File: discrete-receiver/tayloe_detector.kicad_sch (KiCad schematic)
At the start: 22 parts, among them U1 SN74CBT3253DBQR, U2 OPA1612AxD, U3 OPA1612AxD

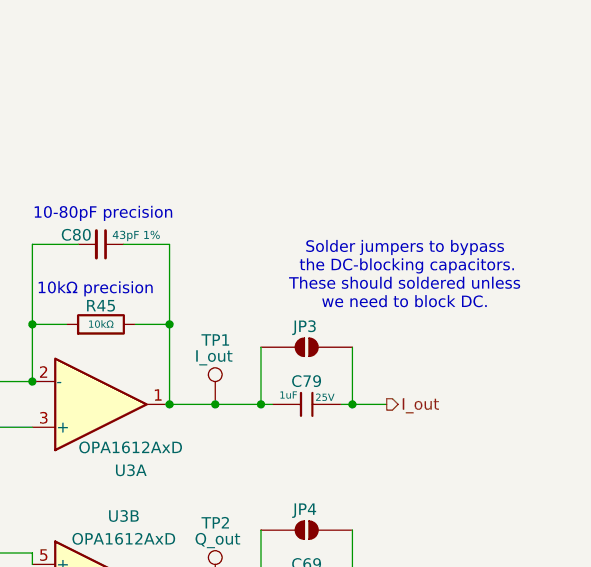
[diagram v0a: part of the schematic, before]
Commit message: Subsheetified the receiver page
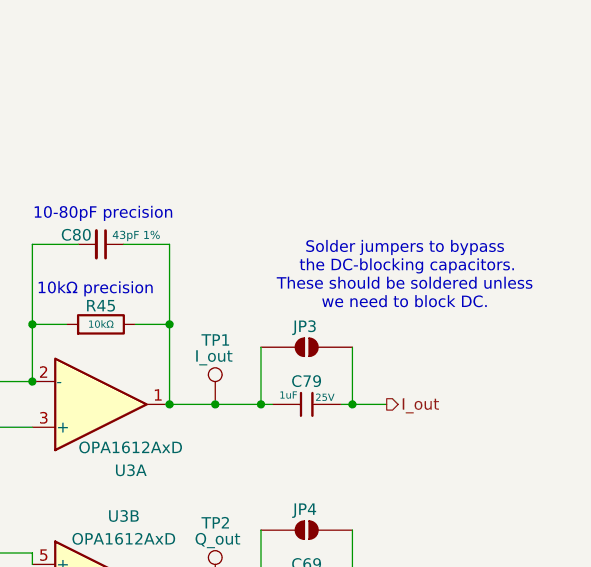
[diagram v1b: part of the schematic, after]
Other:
- note added: "Solder jumpers to bypass the DC-blocking capacitors. These should be soldered unless we need to block DC."
- note removed: "Solder jumpers to bypass the DC-blocking capacitors. These should soldered unless we need to block DC."
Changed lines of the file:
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@@
 		)
 	)
-	(text "Solder jumpers to bypass\n the DC-blocking capacitors.\nThese should soldered unless \nwe need to block DC."
+	(text "Solder jumpers to bypass\n the DC-blocking capacitors.\nThese should be soldered unless \nwe need to block DC."
 		(exclude_from_sim no)
 		(at 226.822 75.946 0)

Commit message: Progress made on schematic
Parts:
- added C8, C83: 100nF, PCM_JLCPCB:C_0402, symbol PCM_JLCPCB-Capacitors:0402,100nF
- added C82, C84: 1uF, PCM_JLCPCB:C_0402, symbol PCM_JLCPCB-Capacitors:0402,1uF
- added JP19, JP23, JP24, JP25: SolderJumper_2_Open, symbol Jumper:SolderJumper_2_Open
- added R48, R49: 10kΩ, PCM_JLCPCB:R_0402, symbol PCM_JLCPCB-Resistors:0402,10kΩ
- added unit 3 of U2
- added unit 3 of U3
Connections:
- net GND: now also C8.2, C82.2, C83.2, C84.2, U2.4 (V-), U3.4 (V-)
- net at C79.1, C80.1, JP3.2 (B)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: now also R48.2
- net at R14.2, R45.1, U3.2 (-): now also JP19.2 (B), JP23.2 (B); no longer C80.2
- net at C69.1, C81.1, JP4.2 (B)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: now also R49.2
- net at R15.2, R44.1, U3.6 (-): now also JP24.2 (B), JP25.2 (B); no longer C81.2
- new net: JP25.1 (A), R49.1
- new net: C80.2, JP23.1 (A)
- new net: JP19.1 (A), R48.1
- new net: C81.2, JP24.1 (A)
- new net VDDA: C8.1, C82.1, C83.1, C84.1, U2.8 (V+), U3.8 (V+)
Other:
- note added: "OPAMP Voltage Rails"
- moved on the sheet: C80

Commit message: Started to redo power
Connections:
- net VDDA renamed +5V_A
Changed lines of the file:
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@@
 			)
 		)
-		(property "Value" "VDDA"
+		(property "Value" "+5V_A"
 			(at 120.65 153.416 0)
 			(show_name no)
@@
 			)
 		)
-		(property "Value" "VDDA"
+		(property "Value" "+5V_A"
 			(at 90.17 153.416 0)
 			(show_name no)
